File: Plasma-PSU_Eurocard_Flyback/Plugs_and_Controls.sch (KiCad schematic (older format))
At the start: 31 parts

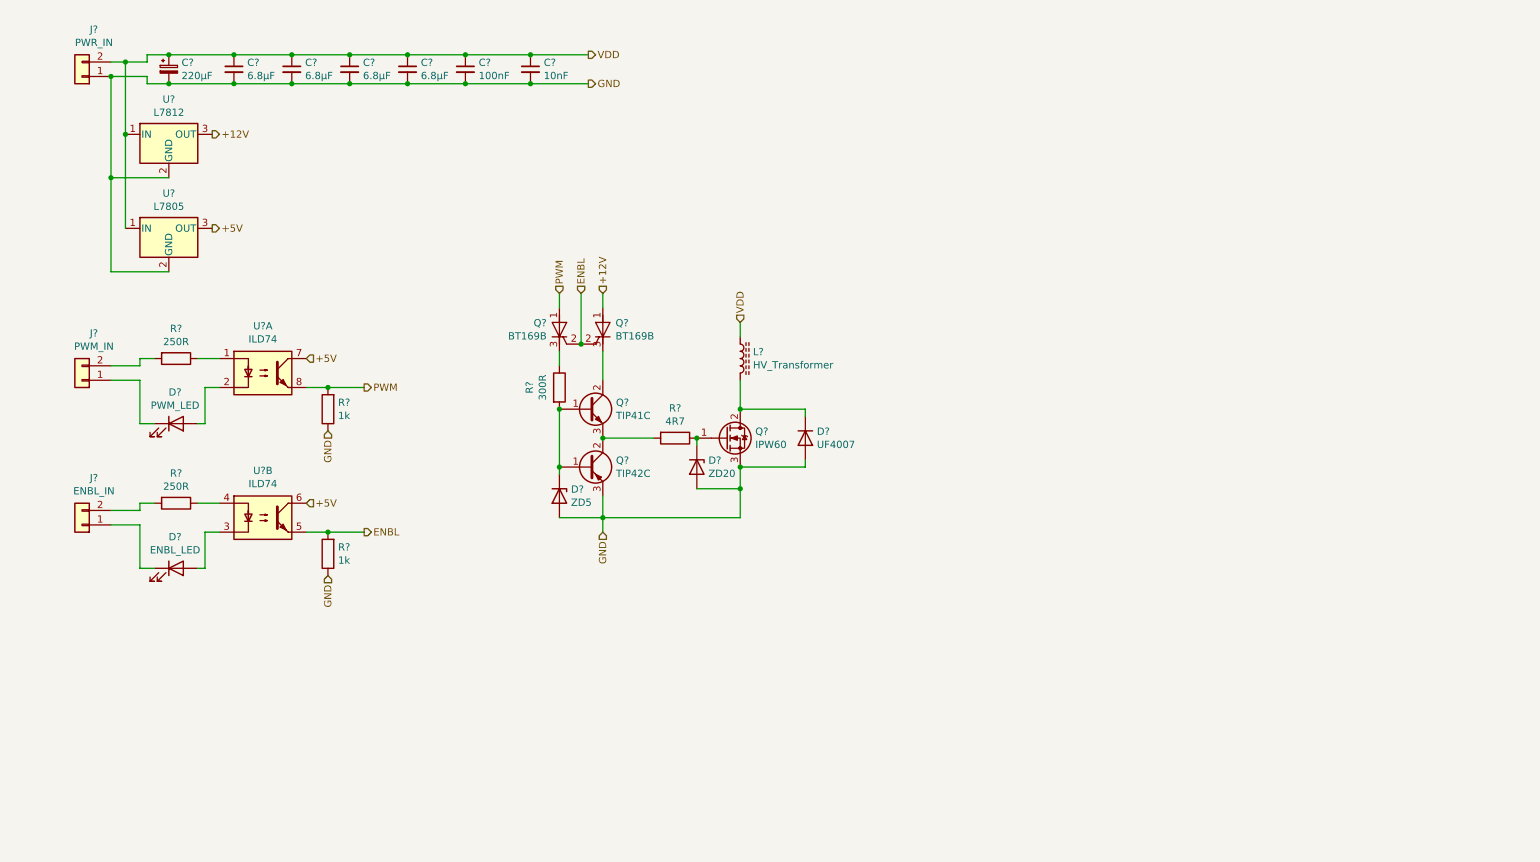
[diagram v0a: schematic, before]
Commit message: Block diagram, Connectivity, Isolation
- First page reservered for block diagram
- Connectors moved to separate sheet
- Opto-isolators for signal inputs on HV board
- Fuse added to SMPS
- Pinheader for Arduino pin-out, UART, I2C, SPI
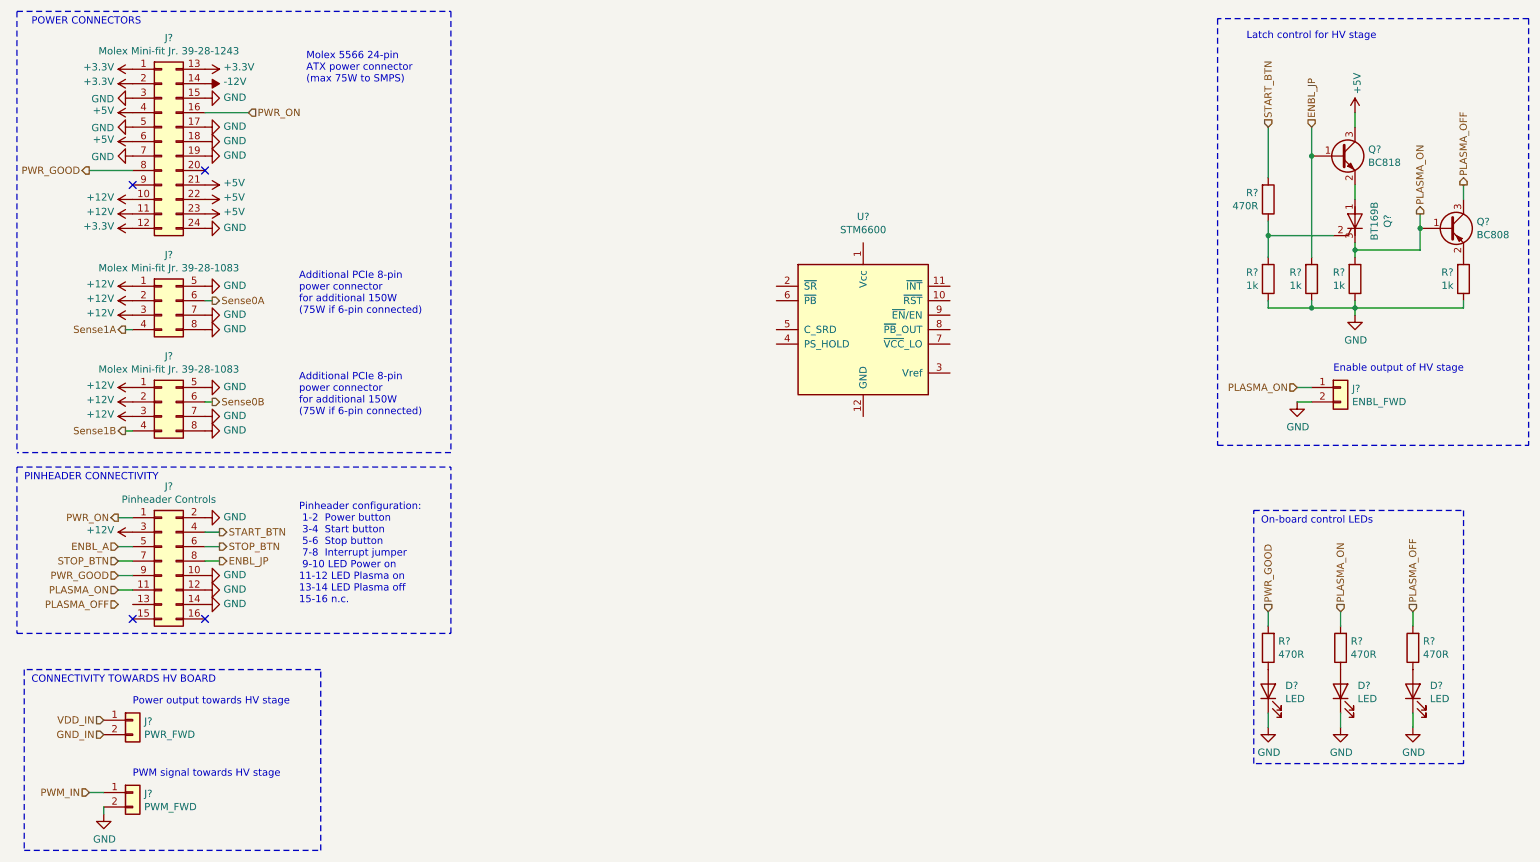
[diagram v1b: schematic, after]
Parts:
- removed C? (x4): 6.8µF, symbol Device:C_Small
- removed C?: 220µF, symbol Device:CP_Small
- removed C?: 100nF, symbol Device:C_Small
- removed C?: 10nF, symbol Device:C_Small
- removed D?: ZD5, Diode_THT:D_DO-41_SOD81_P7.62mm_Horizontal, symbol Device:D_Zener
- removed D?: ZD20, Diode_THT:D_DO-41_SOD81_P7.62mm_Horizontal, symbol Device:D_Zener
- removed D?: UF4007, Diode_THT:D_DO-41_SOD81_P7.62mm_Horizontal, symbol Device:D
- removed D?: PWM_LED, symbol Device:LED
- removed D?: ENBL_LED, symbol Device:LED
- removed J?: PWR_IN, symbol Connector_Generic:Conn_01x02
- removed J?: PWM_IN, symbol Connector_Generic:Conn_01x02
- removed J?: ENBL_IN, symbol Connector_Generic:Conn_01x02
- removed L?: HV_Transformer, Plasma-PSU_Eurocard_Flyback:HF-HV_Transformer_15kV_300W, symbol Device:L_Core_Ferrite
- removed Q? (x2): BT169B, Package_TO_SOT_THT:TO-92_Inline, symbol Triac_Thyristor:BT169B
- removed Q?: TIP41C, Package_TO_SOT_THT:TO-220-3_Vertical, symbol Transistor_BJT:TIP41C
- removed Q?: TIP42C, Package_TO_SOT_THT:TO-220-3_Vertical, symbol Transistor_BJT:TIP42C
- removed Q?: IPW60, Package_TO_SOT_THT:TO-247-3_Vertical, symbol Device:Q_NMOS_GDS
- removed R?: 4R7, Resistor_THT:R_Axial_DIN0207_L6.3mm_D2.5mm_P7.62mm_Horizontal, symbol Device:R
- removed R?: 300R, Resistor_THT:R_Axial_DIN0207_L6.3mm_D2.5mm_P7.62mm_Horizontal, symbol Device:R
- removed R? (x2): 250R, symbol Device:R
- removed R? (x2): 1k, symbol Device:R
- removed U?: L7812, symbol Regulator_Linear:L7812
- removed U?: L7805, symbol Regulator_Linear:L7805
- removed U? (x2): ILD74, symbol Isolator:ILD74
- added D? (x3): LED, symbol Device:LED
- added J?: ENBL_FWD, symbol Connector_Generic:Conn_01x02
- added J?: Pinheader Controls, Connector_PinHeader_2.54mm:PinHeader_2x08_P2.54mm_Vertical, symbol Connector_Generic:Conn_02x08_Odd_Even
- added J? (x2): Molex Mini-fit Jr. 39-28-1083, Connector_Molex:Molex_Mini-Fit_Jr_5566-08A_2x04_P4.20mm_Vertical, symbol Connector_Generic:Conn_02x04_Top_Bottom
- added J?: Molex Mini-fit Jr. 39-28-1243, Connector_Molex:Molex_Mini-Fit_Jr_5566-24A_2x12_P4.20mm_Vertical, symbol Connector_Generic:Conn_02x12_Top_Bottom
- added J?: PWR_FWD, symbol Connector_Generic:Conn_01x02
- added J?: PWM_FWD, symbol Connector_Generic:Conn_01x02
- added Q?: BT169B, Package_TO_SOT_THT:TO-92_Inline, symbol Triac_Thyristor:BT169B
- added Q?: BC808, Package_TO_SOT_SMD:SOT-23, symbol Transistor_BJT:BC808
- added Q?: BC818, Package_TO_SOT_SMD:SOT-23, symbol Transistor_BJT:BC818
- added R? (x4): 1k, symbol Device:R
- added R? (x4): 470R, symbol Device:R
- added U?: STM6600, Package_DFN_QFN:TDFN-12_2x3mm_P0.5mm, symbol Power_Management:STM6600
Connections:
- net +12V: now also J?.1 (Pin_1), J?.1 (Pin_1), J?.10 (Pin_10), J?.11 (Pin_11), J?.2 (Pin_2), J?.2 (Pin_2), J?.3 (Pin_3), J?.3 (Pin_3), J?.3 (Pin_3)
- net +5V: now also J?.21 (Pin_21), J?.22 (Pin_22), J?.23 (Pin_23), J?.4 (Pin_4), J?.6 (Pin_6), Q?.3 (C)
- net GND: now also D?.1 (K), D?.1 (K), D?.1 (K), J?.10 (Pin_10), J?.12 (Pin_12), J?.14 (Pin_14), J?.15 (Pin_15), J?.17 (Pin_17), J?.18 (Pin_18), J?.19 (Pin_19), J?.2 (Pin_2), J?.2 (Pin_2), J?.2 (Pin_2), J?.24 (Pin_24), J?.3 (Pin_3), J?.5 (Pin_5), J?.5 (Pin_5), J?.5 (Pin_5), J?.7 (Pin_7), J?.7 (Pin_7), J?.7 (Pin_7), J?.8 (Pin_8), J?.8 (Pin_8), R?.1, R?.1, R?.1, R?.1
- new net: Q?.1 (A), Q?.2 (E)
- new net: Q?.2 (G), R?.1, R?.2
- new net: D?.2 (A), R?.1 (x3)
- new net: Q?.2 (E), R?.2
- new net +3V3: J?.1 (Pin_1), J?.12 (Pin_12), J?.13 (Pin_13), J?.2 (Pin_2)
- new net -12V: J?.14 (Pin_14)
- new net ENBL_A: J?.5 (Pin_5)
- new net ENBL_JP: J?.8 (Pin_8), Q?.1 (B), R?.2
- new net GND_IN: J?.2 (Pin_2)
- new net PLASMA_OFF: Q?.3 (C), R?.2
- new net PLASMA_ON: J?.1 (Pin_1), J?.11 (Pin_11), Q?.1 (B), Q?.3 (K), R?.2, R?.2
- new net PWM_IN: J?.1 (Pin_1)
- new net PWR_GOOD: J?.8 (Pin_8), J?.9 (Pin_9), R?.2
- new net PWR_ON: J?.1 (Pin_1), J?.16 (Pin_16)
- new net START_BTN: J?.4 (Pin_4), R?.2
- new net STOP_BTN: J?.6 (Pin_6), J?.7 (Pin_7)
- new net Sense0A: J?.6 (Pin_6)
- new net Sense0B: J?.6 (Pin_6)
- new net Sense1A: J?.4 (Pin_4)
- new net Sense1B: J?.4 (Pin_4)
- new net VDD_IN: J?.1 (Pin_1)
- no-connect marks 0 -> 4
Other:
- note added: "Additional PCIe 8-pin \npower connector\nfor additional 150W\n(75W if 6-pin connected)"
- note added: "CONNECTIVITY TOWARDS HV BOARD"
- note added: "Enable output of HV stage"
- note added: "Latch control for HV stage"
- note added: "Molex 5566 24-pin\nATX power connector\n(max 75W to SMPS)"
- note added: "On-board control LEDs"
- note added: "PINHEADER CONNECTIVITY"
- note added: "POWER CONNECTORS"
- note added: "PWM signal towards HV stage"
- note added: "Pinheader configuration:\n 1-2 Power button\n 3-4 Start button\n 5-6 Stop button\n 7-8 Interrupt jumper\n 9-10 LED Power on\n11-12 LED Plasma on\n13-14 LED Plasma off\n15-16 n.c."
- note added: "Power output towards HV stage"

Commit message: STM6600 power-up included
An STM6600 IC is now used to enable stand-by and touch-button operation
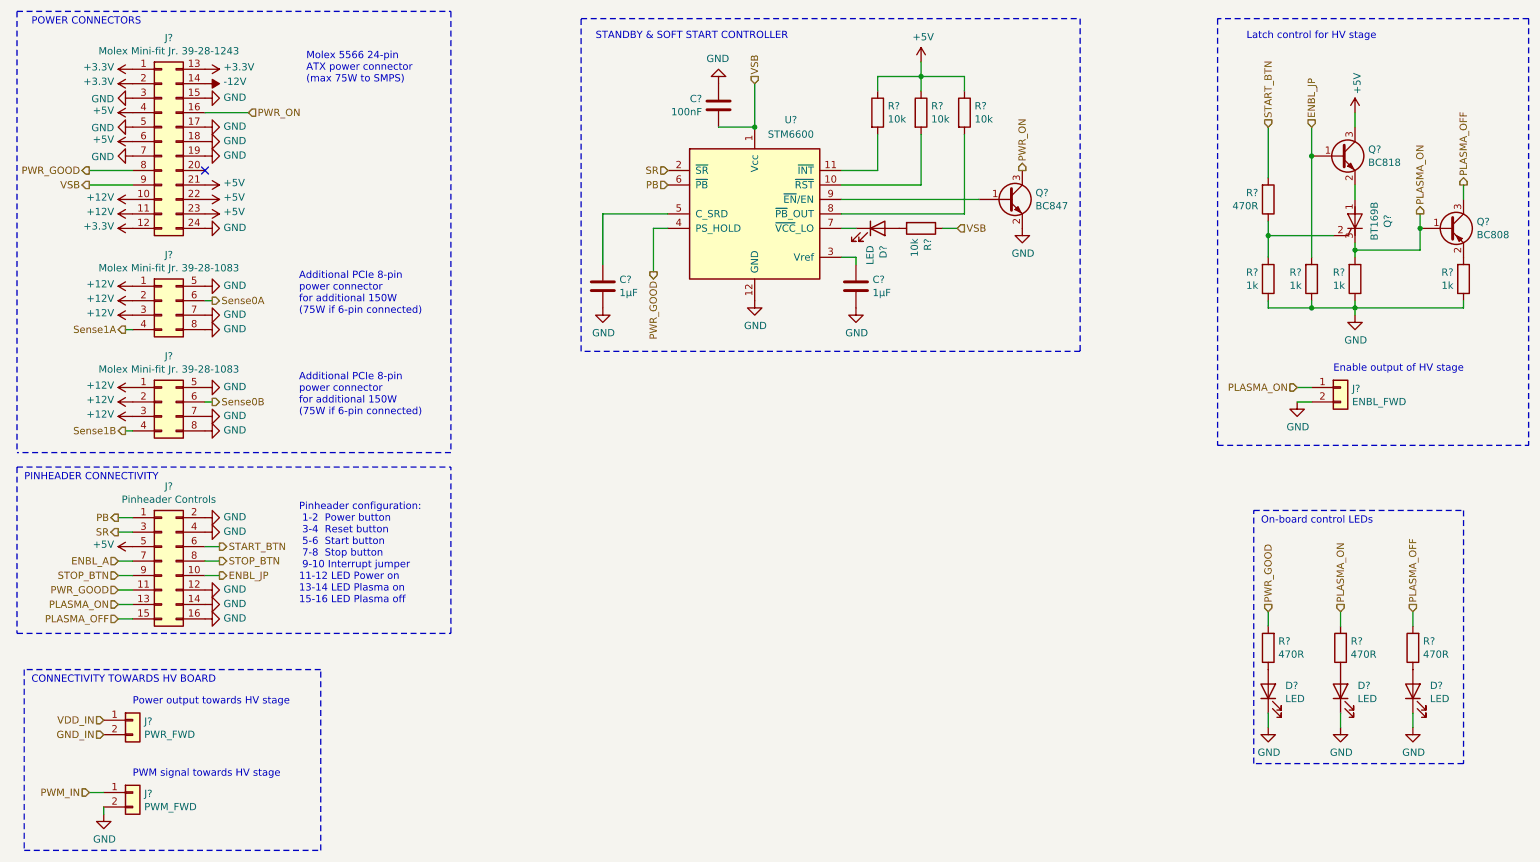
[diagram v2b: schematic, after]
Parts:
- added C?: 100nF, symbol Device:C
- added C? (x2): 1µF, symbol Device:C
- added D?: LED, symbol Device:LED
- added Q?: BC847, Package_TO_SOT_SMD:SOT-23, symbol Transistor_BJT:BC847
- added R? (x4): 10k, symbol Device:R
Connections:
- net +12V: no longer J?.3 (Pin_3)
- net +5V: now also J?.5 (Pin_5), R?.1, R?.1, R?.1
- net ENBL_A: now also J?.7 (Pin_7); no longer J?.5 (Pin_5)
- net ENBL_JP: now also J?.10 (Pin_10); no longer J?.8 (Pin_8)
- net GND: now also J?.16 (Pin_16), J?.4 (Pin_4), U?.12 (GND), C?.2, C?.2, C?.2, Q?.2 (E); no longer J?.10 (Pin_10)
- net PLASMA_OFF: now also J?.15 (Pin_15)
- net PLASMA_ON: now also J?.13 (Pin_13); no longer J?.11 (Pin_11)
- net PWR_GOOD: now also J?.11 (Pin_11), U?.4 (PS_HOLD); no longer J?.9 (Pin_9)
- net PWR_ON: now also Q?.3 (C); no longer J?.1 (Pin_1)
- net START_BTN: now also J?.6 (Pin_6); no longer J?.4 (Pin_4)
- net STOP_BTN: now also J?.8 (Pin_8), J?.9 (Pin_9); no longer J?.6 (Pin_6), J?.7 (Pin_7)
- net VSB: now reaches U?.1 (Vcc)
- net VSB: now also J?.9 (Pin_9), C?.1, R?.1
- net at U?.10 (~RST~): now also R?.2
- net at U?.11 (~INT~): now also R?.2
- net SR: now reaches U?.2 (~SR~)
- net SR: now also J?.3 (Pin_3)
- net at U?.3 (Vref): now also C?.1
- net at U?.5 (C_SRD): now also C?.1
- net PB: now reaches U?.6 (~PB~)
- net PB: now also J?.1 (Pin_1)
- net at U?.7 (~VCC~_LO): now also D?.1 (K)
- net at U?.8 (~PB~_OUT): now also R?.2
- net at U?.9 (~EN~/EN): now also Q?.1 (B)
- new net: D?.2 (A), R?.2
- no-connect marks 4 -> 1
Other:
- note added: "Pinheader configuration:\n 1-2 Power button\n 3-4 Reset button\n 5-6 Start button\n 7-8 Stop button\n 9-10 Interrupt jumper\n11-12 LED Power on\n13-14 LED Plasma on\n15-16 LED Plasma off"
- note added: "STANDBY & SOFT START CONTROLLER"
- note removed: "Pinheader configuration:\n 1-2 Power button\n 3-4 Start button\n 5-6 Stop button\n 7-8 Interrupt jumper\n 9-10 LED Power on\n11-12 LED Plasma on\n13-14 LED Plasma off\n15-16 n.c."
- moved on the sheet: U?

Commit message: Datasheets included
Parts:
- Q?: value BC847 -> BC818
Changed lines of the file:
@@
 P 7450 1900
 F 0 "Q?" H 7641 1946 50  0000 L CNN
-F 1 "BC847" H 7641 1855 50  0000 L CNN
+F 1 "BC818" H 7641 1855 50  0000 L CNN
 F 2 "Package_TO_SOT_SMD:SOT-23" H 7650 1825 50  0001 L CIN
 F 3 "http://www.infineon.com/dgdl/Infineon-BC847SERIES_BC848SERIES_BC849SERIES_BC850SERIES-DS-v01_01-en.pdf?fileId=db3a304314dca389011541d4630a1657" H 7450 1900 50  0001 L CNN

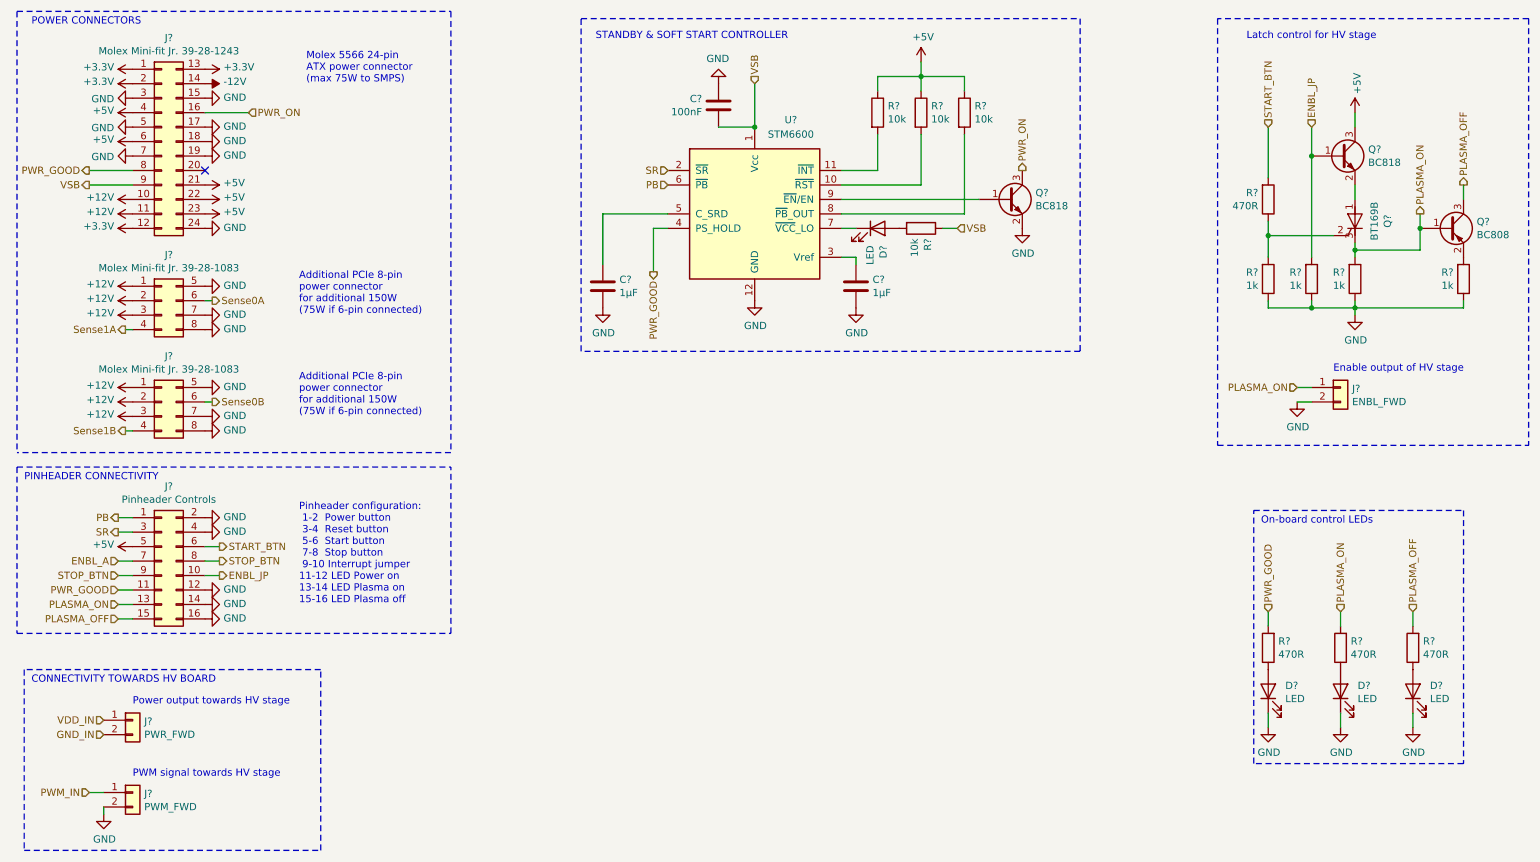
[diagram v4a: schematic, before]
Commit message: Footprints added
All footprints included, except:
- Boost Inductor
- 60A fuse holder
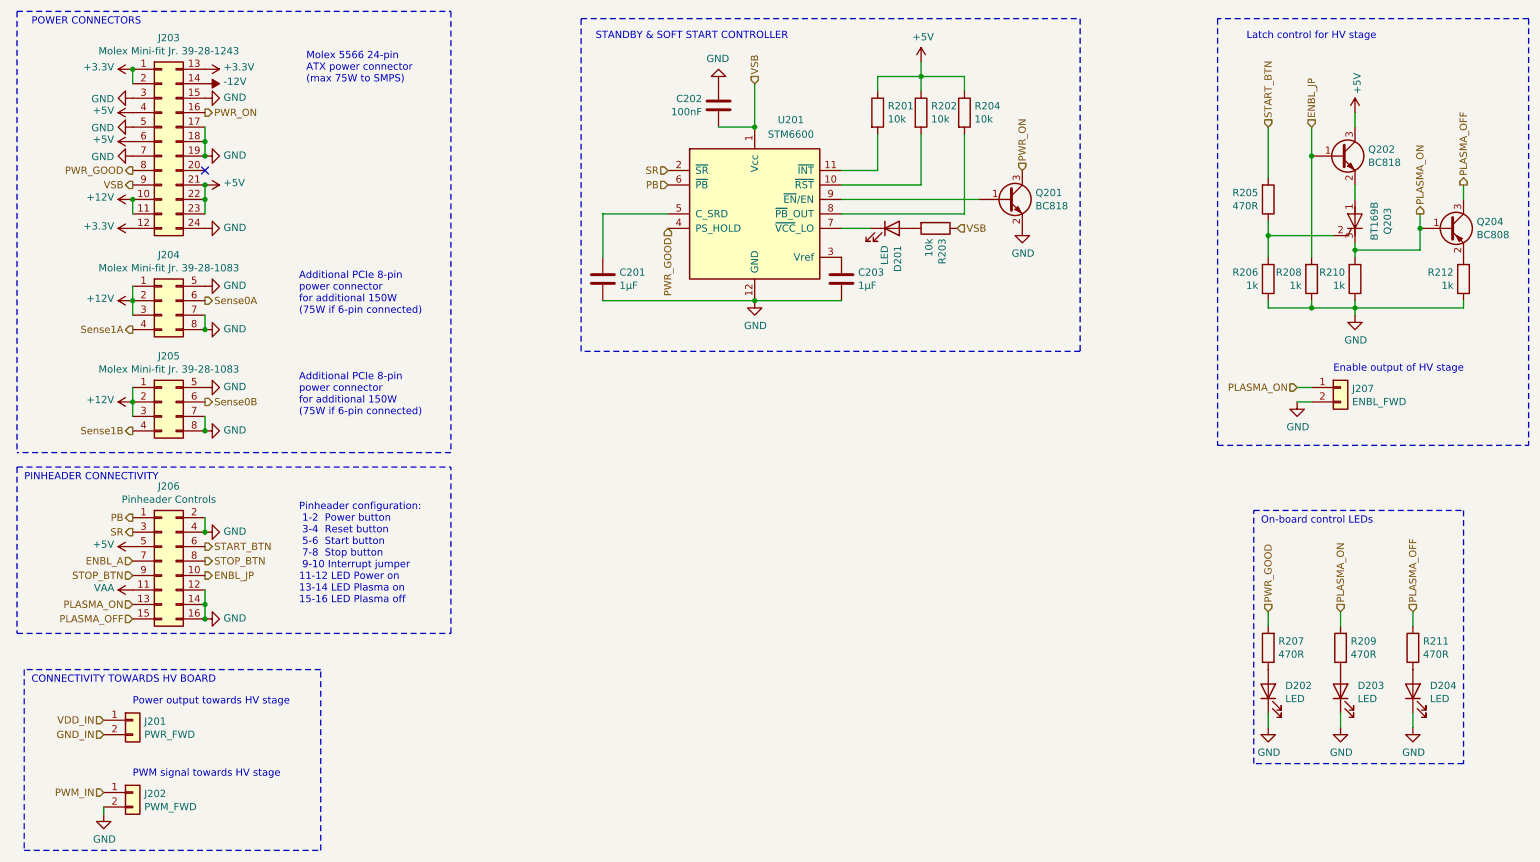
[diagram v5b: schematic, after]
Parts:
- C201, C202, C203: renamed from C?; footprint (none) -> Capacitor_SMD:C_0402_1005Metric
- D201, D202, D203, D204: renamed from D?; footprint (none) -> LED_SMD:LED_0603_1608Metric
- J201: renamed from J?; footprint (none) -> TerminalBlock_Phoenix:TerminalBlock_Phoenix_MKDS-3-2-5.08_1x02_P5.08mm_Horizontal
- J202, J207: renamed from J?; footprint (none) -> Connector_PinSocket_2.54mm:PinSocket_1x02_P2.54mm_Vertical
- R201, R202, R203, R204, R205, R206, R208, R210, R212: renamed from R?; footprint (none) -> Resistor_THT:R_Axial_DIN0207_L6.3mm_D2.5mm_P7.62mm_Horizontal
- R207, R209, R211: renamed from R?; footprint (none) -> Resistor_SMD:R_0402_1005Metric
- gave numbers to parts that had none: 9
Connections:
- net PWR_GOOD: no longer J206.11 (Pin_11)
- new net VAA: J206.11 (Pin_11)
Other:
- moved on the sheet: C201, C203, D201, R203
